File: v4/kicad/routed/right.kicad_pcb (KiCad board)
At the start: 2 copper layers, 160 x 118.6 mm, 72 parts

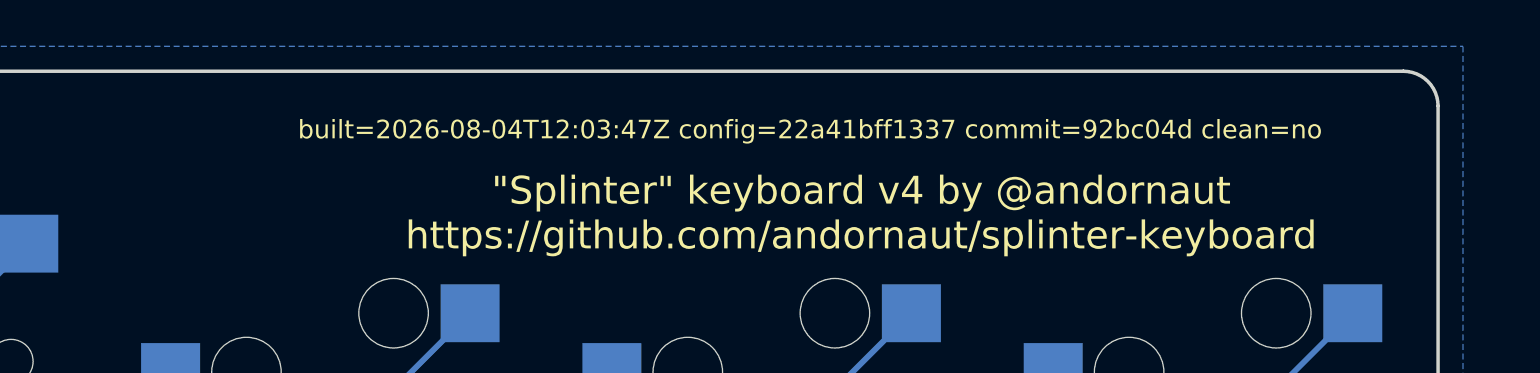
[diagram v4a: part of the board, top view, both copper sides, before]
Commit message: v4: rebuild the boards from a clean tree
Re-stamps all four boards with clean=yes commit=7aa9555, clearing the
two validate:fab non-clean-tree warnings. Copper is unchanged.
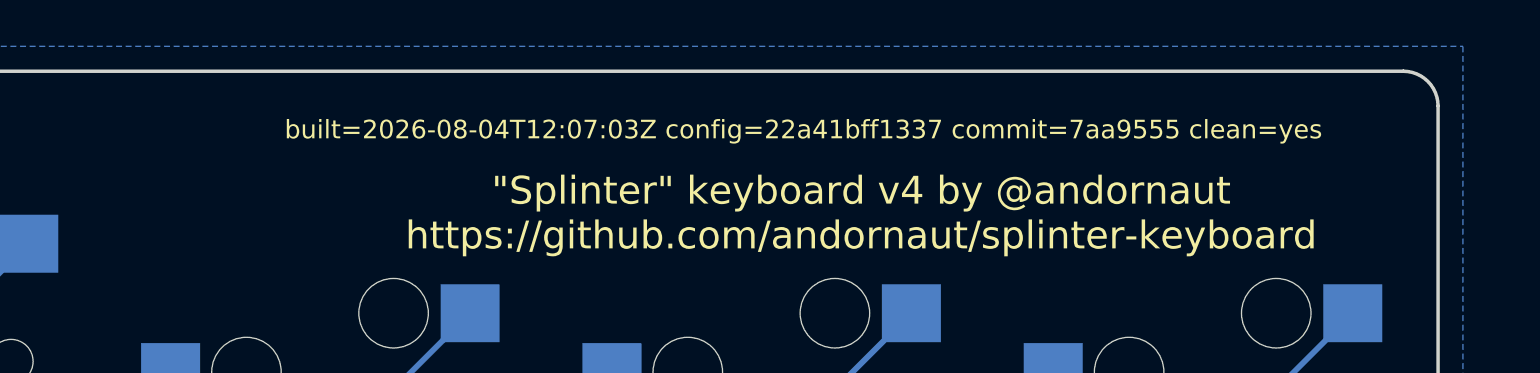
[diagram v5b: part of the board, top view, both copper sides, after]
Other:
- board text added: "built=2026-08-04T12:07:03Z config=22a41bff1337 commit=7aa9555 clean=yes"
- board text removed: "built=2026-08-04T12:03:47Z config=22a41bff1337 commit=92bc04d clean=no"

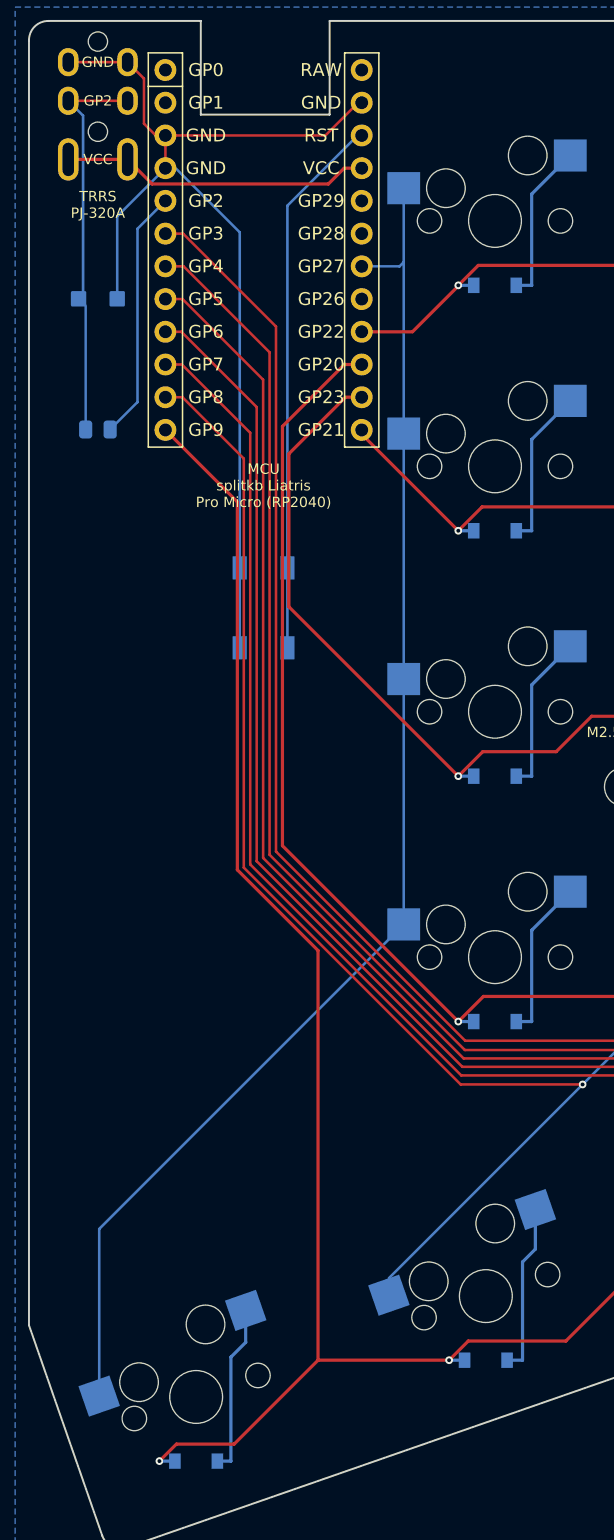
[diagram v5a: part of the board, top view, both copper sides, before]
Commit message: v4: re-route the TRRS data segment on both halves
Re-runs DATA_RAW (TRRS ring 2 to the TVS and the series resistor) on
B.Cu on both halves, and nudges the mirror_five_mod, mirror_four_mod and
MCU GND jogs on the right. DATA_RAW grows 30.99 to 31.98mm (left) and
29.69 to 30.96mm (right); every other net is untouched.

Track count 324 to 327 (left) and 334 to 340 (right), vias 36/38,
teardrops 281/297 and 0 unconnected, all unchanged.
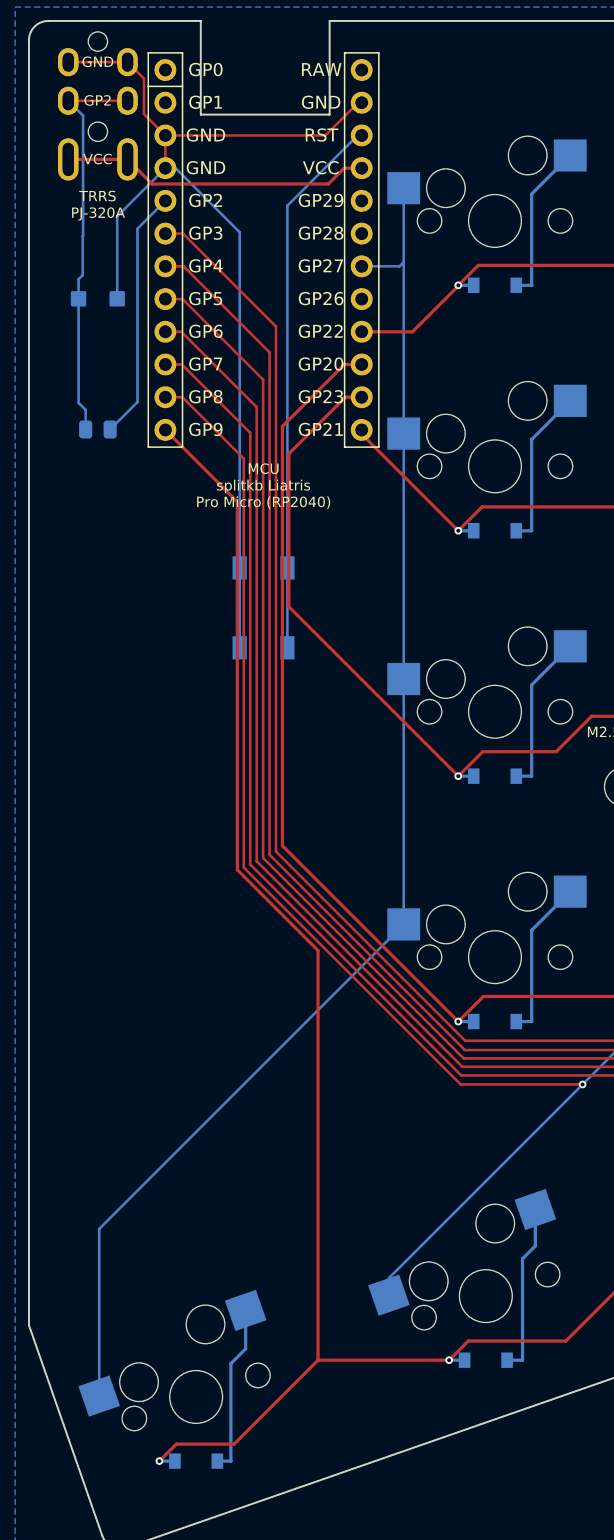
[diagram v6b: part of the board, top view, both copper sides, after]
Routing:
- net DATA_RAW: track 29.7 -> 31.0 mm

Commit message: v4: rebuild the boards from a clean tree
Re-stamps all four boards with clean=yes commit=1db0e07. Copper is
unchanged.
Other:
- board text added: "built=2026-08-04T12:23:37Z config=22a41bff1337 commit=1db0e07 clean=yes"
- board text removed: "built=2026-08-04T12:07:03Z config=22a41bff1337 commit=7aa9555 clean=yes"

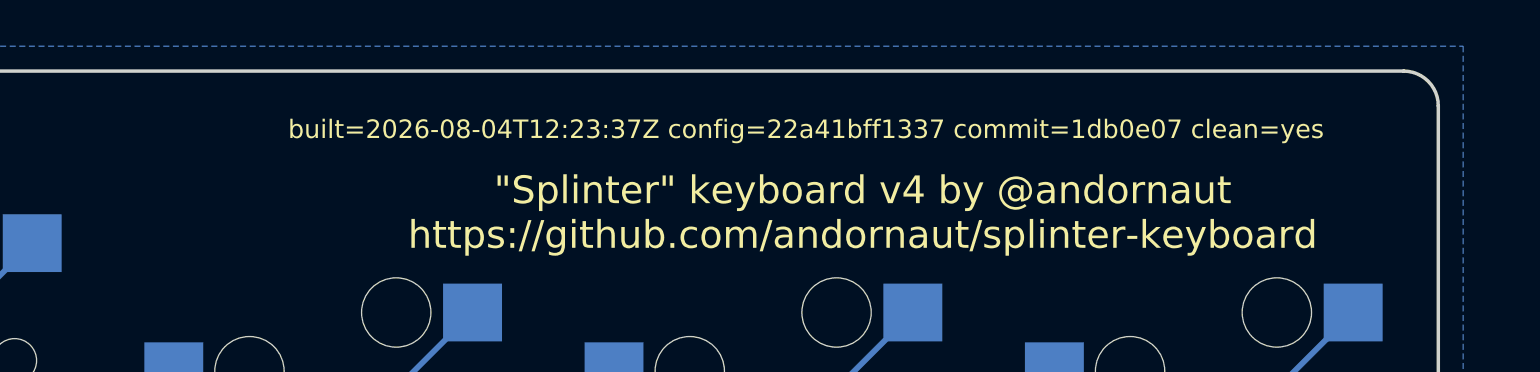
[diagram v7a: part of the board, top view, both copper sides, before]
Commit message: v4: rebuild the boards from a clean tree
Re-stamps all four boards with config=4b4f6b0b9014 clean=yes
commit=dad6706. Copper is unchanged.
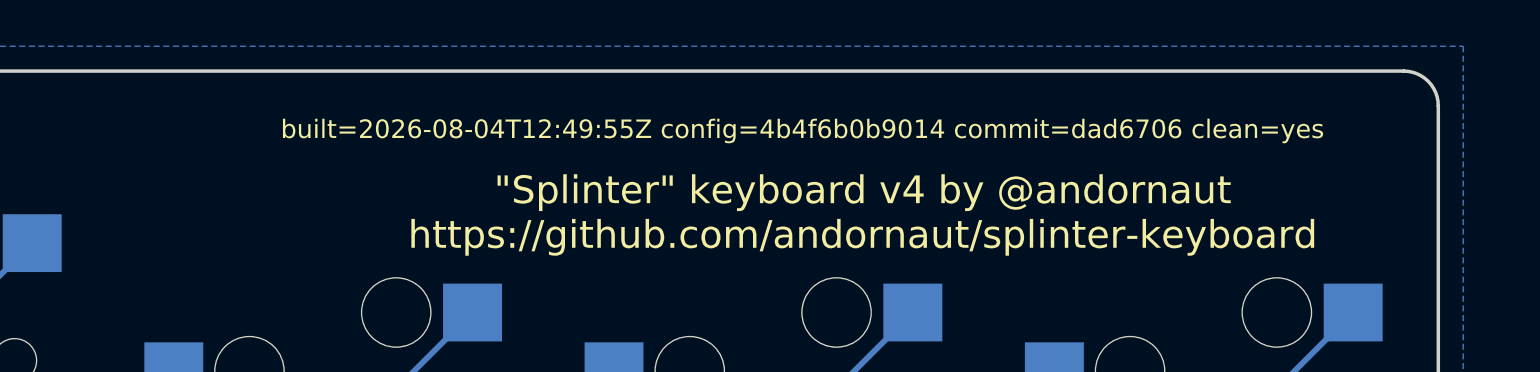
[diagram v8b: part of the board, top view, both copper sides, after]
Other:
- board text added: "built=2026-08-04T12:49:55Z config=4b4f6b0b9014 commit=dad6706 clean=yes"
- board text removed: "built=2026-08-04T12:23:37Z config=22a41bff1337 commit=1db0e07 clean=yes"
